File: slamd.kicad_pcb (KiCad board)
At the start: 2 copper layers, 116.5 x 97 mm, 52 parts, among them J1 CONN_05X2SHD, J2 CONN_05X2SHD, K1 KEYSW, K10 KEYSW, K11 KEYSW, K12 KEYSW, K13 KEYSW, K14 KEYSW, K15 KEYSW, K16 KEYSW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

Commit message: Added mouting holes
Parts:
- added REF**: MountingHole_2.2mm_M2, MountingHole:MountingHole_2.2mm_M2, F.Cu at (124.0, 119.0)
- added REF**: MountingHole_2.2mm_M2, MountingHole:MountingHole_2.2mm_M2, F.Cu at (124.0, 54.0)
- added REF**: MountingHole_2.2mm_M2, MountingHole:MountingHole_2.2mm_M2, F.Cu at (47.6, 53.0)
- added REF**: MountingHole_2.2mm_M2, MountingHole:MountingHole_2.2mm_M2, F.Cu at (47.6, 119.0)
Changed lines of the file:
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@@
-(kicad_pcb (version 20171130) (host pcbnew 5.1.2-1.fc30)
+(kicad_pcb (version 20171130) (host pcbnew "(5.1.5)-3")
   (general
     (thickness 1.6)
     (drawings 9)
-    (tracks 338)
+    (tracks 339)
     (zones 0)
-    (modules 52)
+    (modules 56)
     (nets 47)
   )
@@
     (solder_mask_min_width 0.25)
     (aux_axis_origin 0 0)
-    (visible_elements FFFFFF7F)
+    (visible_elements 7FFFFFFF)
     (pcbplotparams
       (layerselection 0x010fc_ffffffff)
@@
     (add_net "Net-(D9-Pad2)")
   )
+  (module MountingHole:MountingHole_2.2mm_M2 (layer F.Cu)
+    (at 124 119)
+    (descr "Mounting Hole 2.2mm, no annular, M2")
+    (tags "mounting hole 2.2mm no annular m2")
+    (attr virtual)
+    (fp_text reference REF** (at 0 -3.2) (layer F.SilkS)
+      (effects (font (size 1 1) (thickness 0.15)))
+    )
+    (fp_text value MountingHole_2.2mm_M2 (at 0 3.2) (layer F.Fab)
+      (effects (font (size 1 1) (thickness 0.15)))
+    )
+    (fp_text user %R (at 0.3 0) (layer F.Fab)
+      (effects (font (size 1 1) (thickness 0.15)))
+    )
+    (fp_circle (center 0 0) (end 2.2 0) (layer Cmts.User) (width 0.15))
+    (fp_circle (center 0 0) (end 2.45 0) (layer F.CrtYd) (width 0.05))
+    (pad 1 np_thru_hole circle (at 0 0) (size 2.2 2.2) (drill 2.2) (layers *.Cu *.Mask))
+  )
+  (module MountingHole:MountingHole_2.2mm_M2 (layer F.Cu)
+    (at 124 54)
+    (descr "Mounting Hole 2.2mm, no annular, M2")
+    (tags "mounting hole 2.2mm no annular m2")
+    (attr virtual)
+    (fp_text reference REF** (at 0 -3.2) (layer F.SilkS)
+      (effects (font (size 1 1) (thickness 0.15)))
+    )
+    (fp_text value MountingHole_2.2mm_M2 (at 0 3.2) (layer F.Fab)
+      (effects (font (size 1 1) (thickness 0.15)))
+    )
+    (fp_circle (center 0 0) (end 2.45 0) (layer F.CrtYd) (width 0.05))
+    (fp_circle (center 0 0) (end 2.2 0) (layer Cmts.User) (width 0.15))
+    (fp_text user %R (at 0.3 0) (layer F.Fab)
+      (effects (font (size 1 1) (thickness 0.15)))
+    )
+    (pad 1 np_thru_hole circle (at 0 0) (size 2.2 2.2) (drill 2.2) (layers *.Cu *.Mask))
+  )
+  (module MountingHole:MountingHole_2.2mm_M2 (layer F.Cu)
+    (at 47.6 53)
+    (descr "Mounting Hole 2.2mm, no annular, M2")
+    (tags "mounting hole 2.2mm no annular m2")
+    (attr virtual)
+    (fp_text reference REF** (at 0 -3.2) (layer F.SilkS)
+      (effects (font (size 1 1) (thickness 0.15)))
+    )
+    (fp_text value MountingHole_2.2mm_M2 (at 0 3.2) (layer F.Fab)
+      (effects (font (size 1 1) (thickness 0.15)))
+    )
+    (fp_text user %R (at 0.3 0) (layer F.Fab)
+      (effects (font (size 1 1) (thickness 0.15)))
+    )
+    (fp_circle (center 0 0) (end 2.2 0) (layer Cmts.User) (width 0.15))
+    (fp_circle (center 0 0) (end 2.45 0) (layer F.CrtYd) (width 0.05))
+    (pad 1 np_thru_hole circle (at 0 0) (size 2.2 2.2) (drill 2.2) (layers *.Cu *.Mask))
+  )
+  (module MountingHole:MountingHole_2.2mm_M2 (layer F.Cu)
+    (at 47.6 119)
+    (descr "Mounting Hole 2.2mm, no annular, M2")
+    (tags "mounting hole 2.2mm no annular m2")
+    (attr virtual)
+    (fp_text reference REF** (at 0 -3.2) (layer F.SilkS)
+      (effects (font (size 1 1) (thickness 0.15)))
+    )
+    (fp_text value MountingHole_2.2mm_M2 (at 0 3.2) (layer F.Fab)
+      (effects (font (size 1 1) (thickness 0.15)))
+    )
+    (fp_circle (center 0 0) (end 2.45 0) (layer F.CrtYd) (width 0.05))
+    (fp_circle (center 0 0) (end 2.2 0) (layer Cmts.User) (width 0.15))
+    (fp_text user %R (at 0.3 0) (layer F.Fab)
+      (effects (font (size 1 1) (thickness 0.15)))
+    )
+    (pad 1 np_thru_hole circle (at 0 0) (size 2.2 2.2) (drill 2.2) (layers *.Cu *.Mask))
+  )
   (module boards:SPARKFUN_PRO_MICRO (layer F.Cu)
     (at 45.2 38.2 90)
@@
   (segment (start 111.65 65.5) (end 112.775001 66.625001) (width 0.25) (layer F.Cu) (net 3) (status 10))
   (segment (start 110.6 65.5) (end 111.65 65.5) (width 0.25) (layer F.Cu) (net 3) (status 30))
-  (segment (start 47.74 54.330334) (end 47.74 45.82) (width 0.25) (layer F.Cu) (net 3) (status 20))
-  (segment (start 36.570334 65.5) (end 47.74 54.330334) (width 0.25) (layer F.Cu) (net 3) (status 10))
-  (segment (start 34.6 65.5) (end 36.570334 65.5) (width 0.25) (layer F.Cu) (net 3) (status 30))
   (segment (start 71.55 65.5) (end 72.6 65.5) (width 0.25) (layer F.Cu) (net 3) (status 20))
   (segment (start 70.424999 66.625001) (end 71.55 65.5) (width 0.25) (layer F.Cu) (net 3))
   (segment (start 53.675001 66.625001) (end 70.424999 66.625001) (width 0.25) (layer F.Cu) (net 3))
+  (segment (start 44.8 48.76) (end 47.74 45.82) (width 0.25) (layer F.Cu) (net 3))
+  (segment (start 44.8 57.270334) (end 44.8 48.76) (width 0.25) (layer F.Cu) (net 3))
+  (segment (start 34.6 65.5) (end 36.570334 65.5) (width 0.25) (layer F.Cu) (net 3))
+  (segment (start 36.570334 65.5) (end 44.8 57.270334) (width 0.25) (layer F.Cu) (net 3))
   (segment (start 37.46 39.77) (end 37.46 43.46) (width 0.25) (layer F.Cu) (net 4) (status 10))
   (segment (start 47.92 43.46) (end 50.28 45.82) (width 0.25) (layer F.Cu) (net 4) (status 20))

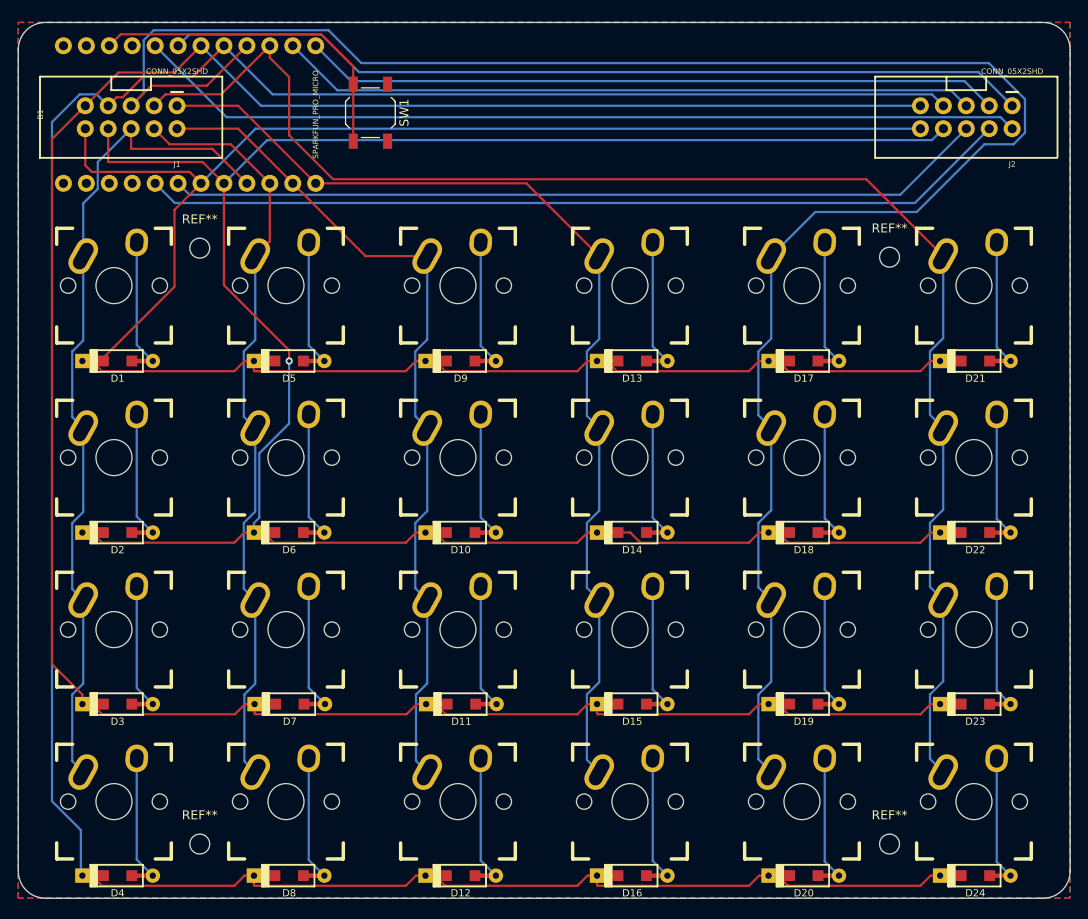
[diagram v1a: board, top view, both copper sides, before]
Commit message: turned 180 degree the left side connector
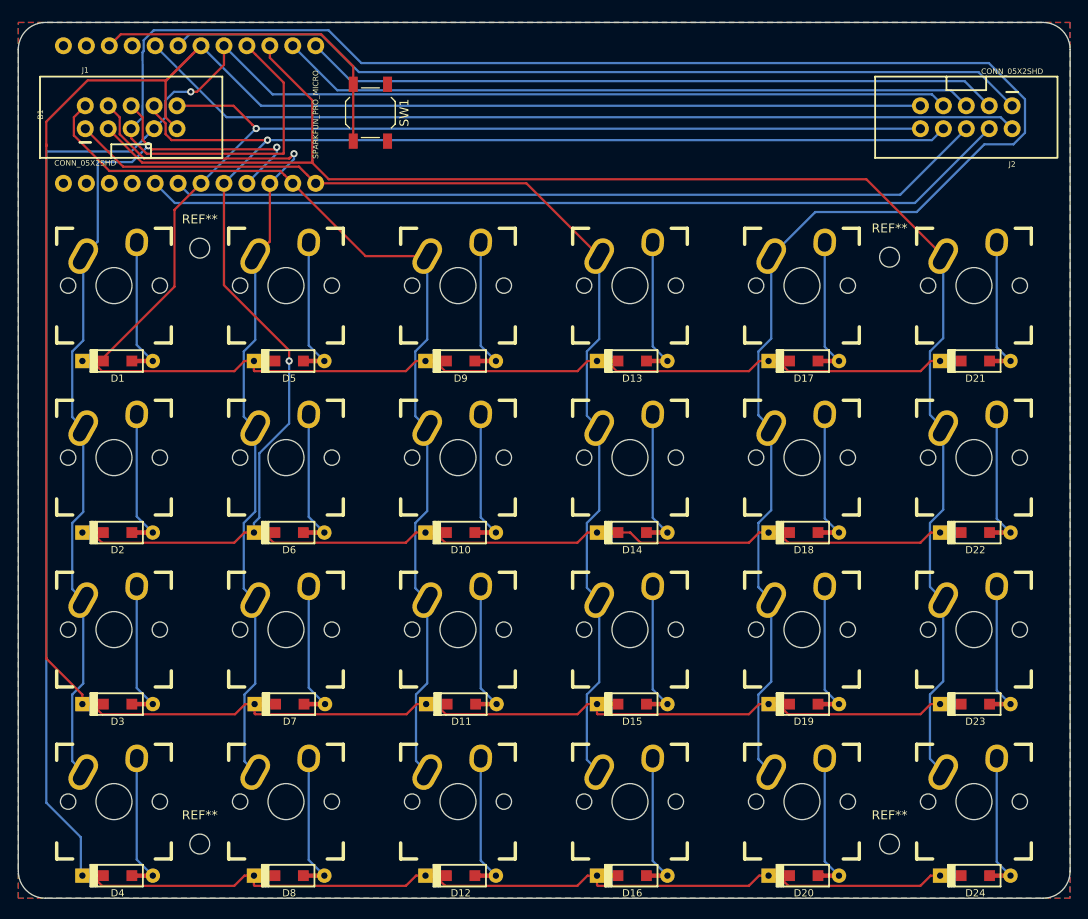
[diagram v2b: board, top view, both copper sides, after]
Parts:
- turned J1 to 90 degrees
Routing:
- net /col4: track 222.8 -> 242.1 mm
- net /col2: track 93.9 -> 108.9 mm
- net /row2: track 268.1 -> 281.6 mm
- net /col1: track 84.3 -> 97.7 mm, vias 0 -> 1
- net /col0: track 93.1 -> 102.7 mm, vias 0 -> 2
- net /col3: track 114.2 -> 123.3 mm
- net /col5: track 165.2 -> 174.0 mm
- net /row0: track 226.4 -> 218.6 mm, vias 0 -> 1
- net /row1: track 242.6 -> 240.4 mm, vias 1 -> 2
- net /row3: track 291.8 -> 292.1 mm, vias 0 -> 1

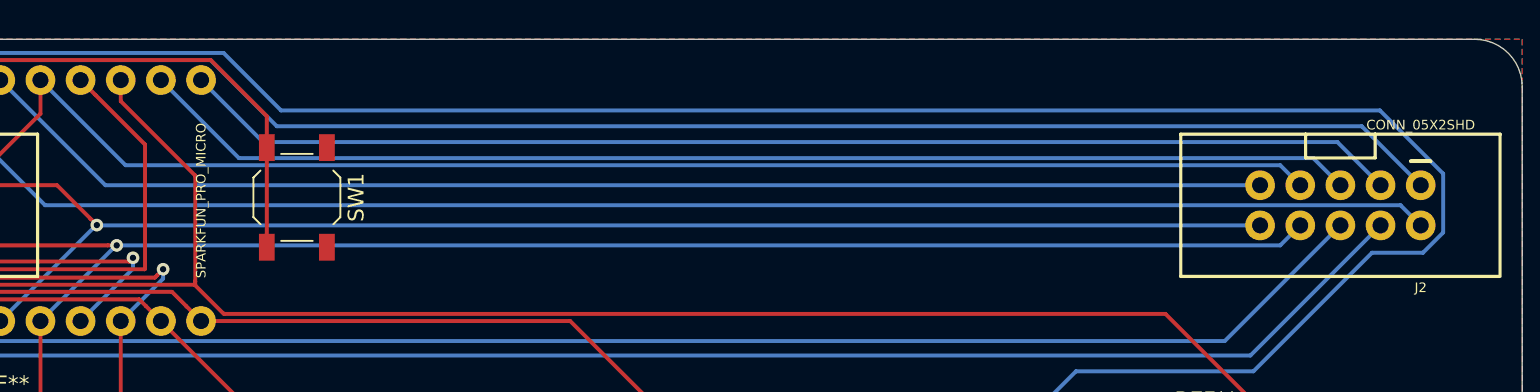
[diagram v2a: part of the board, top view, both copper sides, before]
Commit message: add mouting holes for a protector
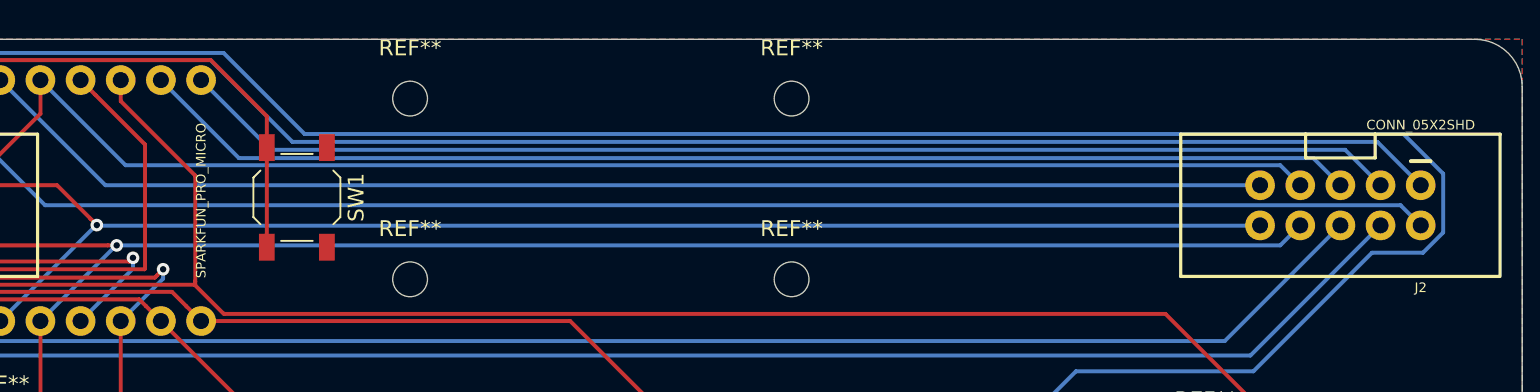
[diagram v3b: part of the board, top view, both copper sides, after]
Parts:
- added REF**: MountingHole_2.2mm_M2, MountingHole:MountingHole_2.2mm_M2, F.Cu at (97.8, 31.8)
- added REF**: MountingHole_2.2mm_M2, MountingHole:MountingHole_2.2mm_M2, F.Cu at (97.8, 43.2)
- added REF**: MountingHole_2.2mm_M2, MountingHole:MountingHole_2.2mm_M2, F.Cu at (73.7, 31.8)
- added REF**: MountingHole_2.2mm_M2, MountingHole:MountingHole_2.2mm_M2, F.Cu at (73.7, 43.2)

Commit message: adjust mounting holes
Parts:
- moved REF** 0.64 mm to (97.8, 31.1)
- moved REF** 0.64 mm to (73.7, 31.1)
- moved REF** 0.63 mm to (97.8, 43.8)
- moved REF** 0.63 mm to (73.7, 43.8)
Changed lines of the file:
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@@
     (thickness 1.6)
     (drawings 9)
-    (tracks 385)
+    (tracks 387)
     (zones 0)
     (modules 60)
@@
   )
   (module MountingHole:MountingHole_2.2mm_M2 (layer F.Cu)
-    (at 97.79 31.75)
+    (at 97.79 31.115)
     (descr "Mounting Hole 2.2mm, no annular, M2")
     (tags "mounting hole 2.2mm no annular m2")
     (attr virtual)
-    (fp_text reference REF** (at 0 -3.2) (layer F.SilkS)
+    (fp_text reference REF** (at 5.2959 0.0508) (layer F.SilkS) hide
       (effects (font (size 1 1) (thickness 0.15)))
     )
@@
   )
   (module MountingHole:MountingHole_2.2mm_M2 (layer F.Cu)
-    (at 97.79 43.18)
+    (at 97.79 43.815)
     (descr "Mounting Hole 2.2mm, no annular, M2")
     (tags "mounting hole 2.2mm no annular m2")
     (attr virtual)
-    (fp_text reference REF** (at 0 -3.2) (layer F.SilkS)
+    (fp_text reference REF** (at 5.6261 -0.0127) (layer F.SilkS) hide
       (effects (font (size 1 1) (thickness 0.15)))
     )
@@
   )
   (module MountingHole:MountingHole_2.2mm_M2 (layer F.Cu)
-    (at 73.66 31.75)
+    (at 73.66 31.115)
     (descr "Mounting Hole 2.2mm, no annular, M2")
     (tags "mounting hole 2.2mm no annular m2")
     (attr virtual)
-    (fp_text reference REF** (at 0 -3.2) (layer F.SilkS)
+    (fp_text reference REF** (at 5.3467 0) (layer F.SilkS) hide
       (effects (font (size 1 1) (thickness 0.15)))
     )
@@
   )
   (module MountingHole:MountingHole_2.2mm_M2 (layer F.Cu)
-    (at 73.66 43.18)
+    (at 73.66 43.815)
     (descr "Mounting Hole 2.2mm, no annular, M2")
     (tags "mounting hole 2.2mm no annular m2")
     (attr virtual)
-    (fp_text reference REF** (at 0 -3.2) (layer F.SilkS)
+    (fp_text reference REF** (at 5.2324 -0.0381) (layer F.SilkS) hide
       (effects (font (size 1 1) (thickness 0.15)))
     )
@@
     (tags "mounting hole 2.2mm no annular m2")
     (attr virtual)
-    (fp_text reference REF** (at 0 -3.2) (layer F.SilkS)
+    (fp_text reference REF** (at 0 -3.2) (layer F.SilkS) hide
       (effects (font (size 1 1) (thickness 0.15)))
     )
@@
     (tags "mounting hole 2.2mm no annular m2")
     (attr virtual)
-    (fp_text reference REF** (at 0 -3.2) (layer F.SilkS)
+    (fp_text reference REF** (at 0 -3.2) (layer F.SilkS) hide
       (effects (font (size 1 1) (thickness 0.15)))
     )
@@
     (tags "mounting hole 2.2mm no annular m2")
     (attr virtual)
-    (fp_text reference REF** (at 0 -3.2) (layer F.SilkS)
+    (fp_text reference REF** (at 0 -3.2) (layer F.SilkS) hide
       (effects (font (size 1 1) (thickness 0.15)))
     )
@@
     (tags "mounting hole 2.2mm no annular m2")
     (attr virtual)
-    (fp_text reference REF** (at 0 -3.2) (layer F.SilkS)
+    (fp_text reference REF** (at 0 -3.2) (layer F.SilkS) hide
       (effects (font (size 1 1) (thickness 0.15)))
     )
@@
   (segment (start 91.845 101.069998) (end 90.474999 102.439999) (width 0.25) (layer B.Cu) (net 8))
   (segment (start 91.845 91.98) (end 91.845 101.069998) (width 0.25) (layer B.Cu) (net 8) (status 10))
-  (segment (start 83.785 45.82) (end 91.845 53.88) (width 0.25) (layer F.Cu) (net 8) (status 20))
-  (segment (start 60.44 45.82) (end 83.785 45.82) (width 0.25) (layer F.Cu) (net 8) (status 10))
   (segment (start 39.124013 43.974013) (end 58.594013 43.974013) (width 0.25) (layer F.Cu) (net 8))
   (segment (start 58.594013 43.974013) (end 59.500201 44.880201) (width 0.25) (layer F.Cu) (net 8))
   (segment (start 34.92 39.77) (end 39.124013 43.974013) (width 0.25) (layer F.Cu) (net 8))
   (segment (start 59.500201 44.880201) (end 60.44 45.82) (width 0.25) (layer F.Cu) (net 8))
+  (segment (start 61.379799 46.759799) (end 84.724799 46.759799) (width 0.25) (layer F.Cu) (net 8))
+  (segment (start 60.44 45.82) (end 61.379799 46.759799) (width 0.25) (layer F.Cu) (net 8))
+  (segment (start 84.724799 46.759799) (end 90.925726 52.960726) (width 0.25) (layer F.Cu) (net 8))
+  (segment (start 90.925726 52.960726) (end 91.845 53.88) (width 0.25) (layer F.Cu) (net 8))
   (segment (start 128.474999 71.459999) (end 129.945 72.93) (width 0.25) (layer B.Cu) (net 9) (status 20))
   (segment (start 128.474999 64.439999) (end 128.474999 71.459999) (width 0.25) (layer B.Cu) (net 9))
@@
   (segment (start 60.071 43.491004) (end 60.071 43.307) (width 0.25) (layer F.Cu) (net 9))
   (segment (start 60.038002 43.524002) (end 60.071 43.491004) (width 0.25) (layer F.Cu) (net 9))
-  (segment (start 129.945 53.88) (end 121.43499 45.36999) (width 0.25) (layer F.Cu) (net 9))
-  (segment (start 61.88399 45.36999) (end 60.038002 43.524002) (width 0.25) (layer F.Cu) (net 9))
-  (segment (start 121.43499 45.36999) (end 61.88399 45.36999) (width 0.25) (layer F.Cu) (net 9))
   (segment (start 41.214002 43.524002) (end 60.038002 43.524002) (width 0.25) (layer F.Cu) (net 9))
   (segment (start 37.46 39.77) (end 41.214002 43.524002) (width 0.25) (layer F.Cu) (net 9))
+  (segment (start 122.3438 46.2788) (end 62.7928 46.2788) (width 0.25) (layer F.Cu) (net 9))
+  (segment (start 129.945 53.88) (end 122.3438 46.2788) (width 0.25) (layer F.Cu) (net 9))
+  (segment (start 62.7928 46.2788) (end 60.038002 43.524002) (width 0.25) (layer F.Cu) (net 9))
   (segment (start 109.474999 71.509999) (end 110.895 72.93) (width 0.25) (layer B.Cu) (net 10) (status 20))
   (segment (start 109.474999 64.439999) (end 109.474999 71.509999) (width 0.25) (layer B.Cu) (net 10))

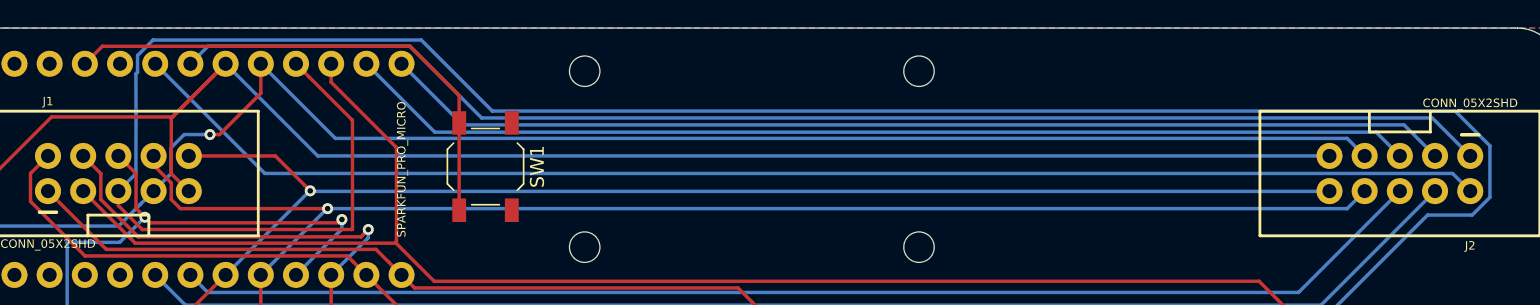
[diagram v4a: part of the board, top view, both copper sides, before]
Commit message: change reset sw
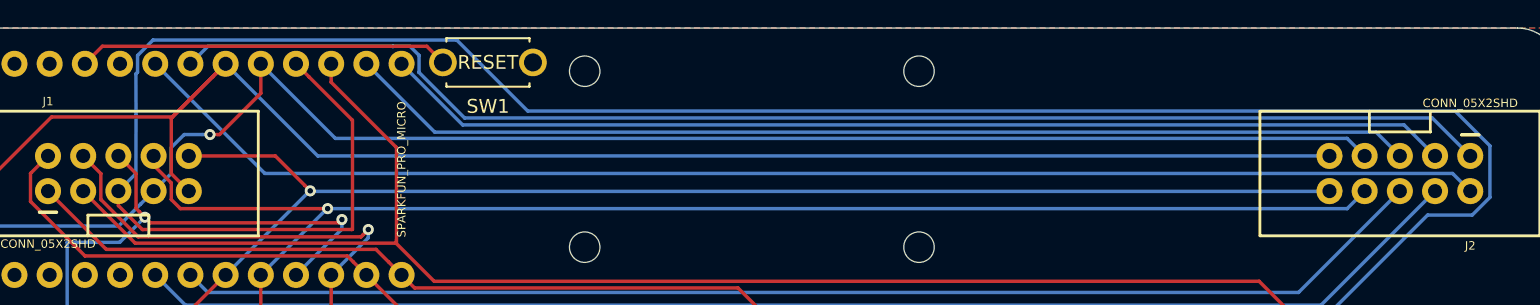
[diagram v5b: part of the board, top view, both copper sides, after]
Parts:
- SW1: footprint Button_Switch_SMD:SW_SPST_TL3342 -> kbd:ResetSW
- moved SW1 7.52 mm to (66.7, 30.5), turned to 0 degrees
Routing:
- net /rst: track 37.3 -> 26.9 mm
- net /col8: track 96.2 -> 96.9 mm
